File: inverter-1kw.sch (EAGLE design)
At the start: 190 parts, among them IC1 LMV358MMX, IC2 LMV358MMX, Q4 1200980569**TRANS SMD NPN MMB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, Q6 1200980569**TRANS SMD NPN MMB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, U1 ACS712, U4 ACS712, U5 SI8230, U6 SI8230, U7 ACS712, X2 https://ozdisan.com/connector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, X3 https://ozdisan.com/connector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, X7 https://ozdisan.com/connector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, X8 https://ozdisan.com/connector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

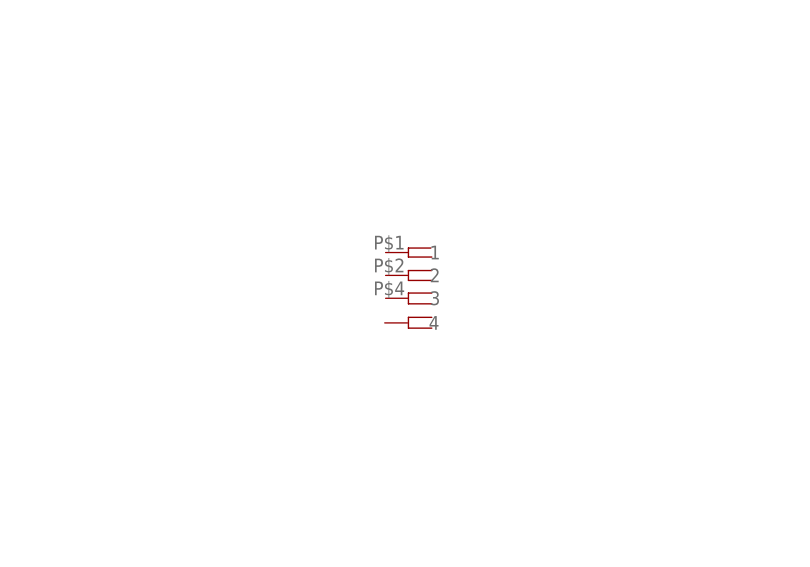
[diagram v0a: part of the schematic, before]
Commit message: Common Filter devresi düzenlendi
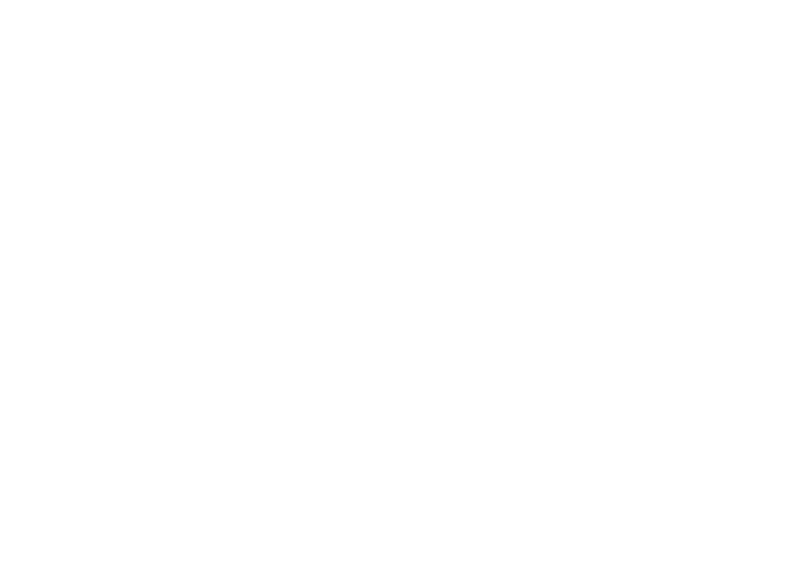
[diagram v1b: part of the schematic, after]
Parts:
- removed U$1: (no value), Andromeda:SCREWCONNECTORS(K93-01AH)
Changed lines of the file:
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@@
 <part name="C48" library="rcl" library_urn="urn:adsk.eagle:library:27228982" deviceset="C-EU" device="C1206" package3d_urn="urn:adsk.eagle:package:27228997/1"/>
 <part name="C49" library="rcl" library_urn="urn:adsk.eagle:library:27228982" deviceset="C-EU" device="C1206" package3d_urn="urn:adsk.eagle:package:27228997/1" value="22p"/>
-<part name="U$1" library="Andromeda" deviceset="SCREWCONNECTORS(K93-01AH)" device=""/>
 </parts>
 <sheets>
@@
 <attribute name="VALUE" x="494.284" y="88.011" size="1.778" layer="96"/>
 </instance>
-<instance part="U$1" gate="G$1" x="290.83" y="337.82" smashed="yes"/>
 </instances>
 <busses>

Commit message: Giris ve cikis guc terminalleri degistirildi.
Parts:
- removed X2, X3, X7, X8: https://ozdisan.com/connectors-and-interconnects/terminals/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, enko:RADE2
- added U$1, U$2, U$3, U$4: (no value), Andromeda:SCREWCONNECTORS(K93-01AH)
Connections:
- net AGND: now also U$2.1, U$2.2, U$2.3, U$2.4; no longer X8.1, X8.2
- net VA_OUT: now also U$4.1, U$4.2, U$4.3, U$4.4; no longer X3.1, X3.2
- net VB_OUT: now also U$3.1, U$3.2, U$3.3, U$3.4; no longer X2.1, X2.2
- net VSUPPLY+: now also U$1.1, U$1.2, U$1.3, U$1.4; no longer X7.1, X7.2

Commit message: Filtre devresi ve opamp devresi düzenlendi.
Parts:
- removed U$1, U$4: (no value), Andromeda:SCREWCONNECTORS(K93-01AH)
- added U$5, U$6: (no value), Andromeda:SCREWCONNECTORS(K93-01AH)
- renumbered U$3 to U$7
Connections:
- new net N$39: C32.-, C33.-, C35.-, C37.2, C40.-, C43.2, C47.2, C48.2, C49.2, C89.2, C90.2, GN4.S, LED5.C, R28.1, R67.1, R96.1, RGND1.2, U$5.1, U$5.2, U$5.3, U$5.4, U6.GNDB
- net AGND: no longer C32.-, C33.-, C35.-, C37.2, C40.-, C43.2, C47.2, C48.2, C49.2, C89.2, C90.2, GN4.S, LED5.C, R28.1, R67.1, R96.1, RGND1.2, U$2.1, U$2.2, U$2.3, U$2.4, U6.GNDB
- net VA_OUT: now also U$6.1, U$6.2, U$6.3, U$6.4; no longer U$4.1, U$4.2, U$4.3, U$4.4
- net VSUPPLY+: now also U$2.1, U$2.2, U$2.3, U$2.4; no longer U$1.1, U$1.2, U$1.3, U$1.4

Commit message: Soket baglantilari duzenlendi. B kol mosfetin AGND baglantisi duzeltildi.
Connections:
- removed net FAN: SV1.14
- removed net N$39: C32.-, C33.-, C35.-, C37.2, C40.-, C43.2, C47.2, C48.2, C49.2, C89.2, C90.2, GN4.S, LED5.C, R28.1, R67.1, R96.1, RGND1.2, U$5.1, U$5.2, U$5.3, U$5.4, U6.GNDB
- removed net N$83: R78.1, R79.2, U5.DISABLE
- removed net N$88: R84.1, R85.2, U6.DISABLE
- removed net NTC-HS1: SV1.16
- removed net NTC-HS2: SV1.18
- new net DRV1_EN: R78.1, R79.2, SV1.9, U5.DISABLE
- new net DRV2_EN: R84.1, R85.2, SV1.15, U6.DISABLE
- new net N$38: SV1.8
- net +3V3: now also SV1.17
- net +5V: now also SV1.19
- net AGND: now also C32.-, C33.-, C35.-, C37.2, C40.-, C43.2, C47.2, C48.2, C49.2, C89.2, C90.2, GN4.S, LED5.C, R28.1, R67.1, R96.1, RGND1.2, U$5.1, U$5.2, U$5.3, U$5.4, U6.GNDB
- net DGND: now also SV1.20
- net G11_PWM: now also SV1.5; no longer SV1.2
- net G12_PWM: now also SV1.7; no longer SV1.4
- net G13_PWM: now also SV1.11; no longer SV1.6
- net G14_PWM: now also SV1.13; no longer SV1.8
- net IA_SENS: now also SV1.14; no longer SV1.9
- net IB_SENS: now also SV1.18; no longer SV1.11
- net IIN_SENS: now also SV1.3; no longer SV1.5
- net RELAY1: now also SV1.2; no longer SV1.10
- net RELAY2: now also SV1.4; no longer SV1.12
- net VA_SENS: now also SV1.12; no longer SV1.13
- net VB_SENS: now also SV1.16; no longer SV1.15
- net VIN_SENS: now also SV1.1; no longer SV1.7
- net VIN_SENS_DIFF: now also SV1.10; no longer SV1.3
- net VOUT_SENS_DIFF: now also SV1.6; no longer SV1.1
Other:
- note added: "220AC"
- note removed: "Maks - 100V"

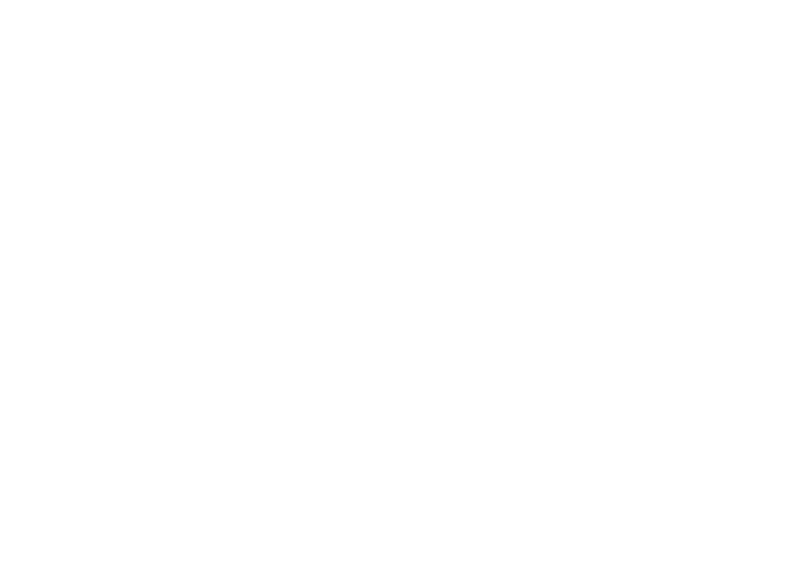
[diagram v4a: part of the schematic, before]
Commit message: ölçüm devresi düzenlendi
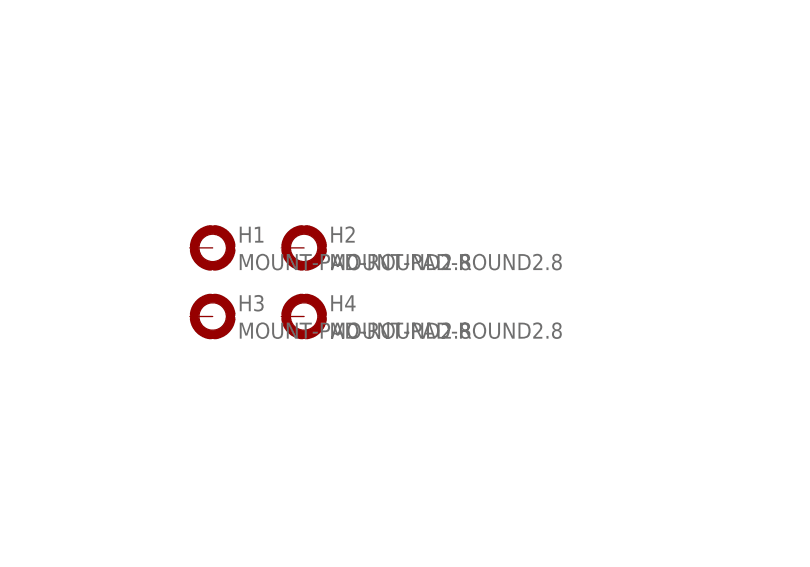
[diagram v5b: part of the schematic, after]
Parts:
- added H1, H2, H3, H4: MOUNT-PAD-ROUND2.8, holes:MOUNT-PAD-ROUND2.8
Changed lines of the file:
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@@
 <part name="U$6" library="Andromeda" library_urn="urn:adsk.eagle:library:27258842" deviceset="SCREWCONNECTORS(K93-01AH)" device="" package3d_urn="urn:adsk.eagle:package:27281814/2"/>
 <part name="U$7" library="Andromeda" library_urn="urn:adsk.eagle:library:27258842" deviceset="SCREWCONNECTORS(K93-01AH)" device="" package3d_urn="urn:adsk.eagle:package:27281814/2"/>
+<part name="H1" library="holes" library_urn="urn:adsk.eagle:library:237" deviceset="MOUNT-PAD-ROUND" device="2.8" package3d_urn="urn:adsk.eagle:package:14281/1"/>
+<part name="H2" library="holes" library_urn="urn:adsk.eagle:library:237" deviceset="MOUNT-PAD-ROUND" device="2.8" package3d_urn="urn:adsk.eagle:package:14281/1"/>
+<part name="H3" library="holes" library_urn="urn:adsk.eagle:library:237" deviceset="MOUNT-PAD-ROUND" device="2.8" package3d_urn="urn:adsk.eagle:package:14281/1"/>
+<part name="H4" library="holes" library_urn="urn:adsk.eagle:library:237" deviceset="MOUNT-PAD-ROUND" device="2.8" package3d_urn="urn:adsk.eagle:package:14281/1"/>
 </parts>
 <sheets>
@@
 <instance part="U$6" gate="G$1" x="816.61" y="226.06" smashed="yes"/>
 <instance part="U$7" gate="G$1" x="817.88" y="116.84" smashed="yes"/>
+<instance part="H1" gate="G$1" x="417.83" y="-13.97" smashed="yes">
+<attribute name="NAME" x="420.624" y="-13.3858" size="1.778" layer="95"/>
+<attribute name="VALUE" x="420.624" y="-16.4338" size="1.778" layer="96"/>
+</instance>
+<instance part="H2" gate="G$1" x="427.99" y="-13.97" smashed="yes">
+<attribute name="NAME" x="430.784" y="-13.3858" size="1.778" layer="95"/>
+<attribute name="VALUE" x="430.784" y="-16.4338" size="1.778" layer="96"/>
+</instance>
+<instance part="H3" gate="G$1" x="417.83" y="-21.59" smashed="yes">
+<attribute name="NAME" x="420.624" y="-21.0058" size="1.778" layer="95"/>
+<attribute name="VALUE" x="420.624" y="-24.0538" size="1.778" layer="96"/>
+</instance>
+<instance part="H4" gate="G$1" x="427.99" y="-21.59" smashed="yes">
+<attribute name="NAME" x="430.784" y="-21.0058" size="1.778" layer="95"/>
+<attribute name="VALUE" x="430.784" y="-24.0538" size="1.778" layer="96"/>
+</instance>
 </instances>
 <busses>

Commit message: Giris ve giris terminalleri soket yapildi. Ganlarin dibindeki capler sadelestirildi.
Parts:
- removed C43: (no value), rcl:C-EUC2220K
- removed D1, D2: (no value), diode:DIODE-SOD123
- removed Q4, Q6: 1200980569**TRANS SMD NPN MMBTA06 SOT-23 80V 500mA, transistor-npn:BC846ALT1SMD
- removed R32, R37, R42, R43: (no value), rcl:R-EU_0411/12
- removed R36, R41: (no value), rcl:R-EU_R0603
- removed RL1, RL2: 0417, Erelay:0417
- removed U$2, U$5, U$6, U$7: (no value), Andromeda:SCREWCONNECTORS(K93-01AH)
- added X1: GMSTBV3, con-phoenix-762:GMSTBV3
- added X2: MSTBV2, con-phoenix-508:MSTBV2
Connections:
- removed net N$14: C42.2, C43.1
- removed net N$22: C28.1, C30.2
- removed net N$32: C29.1, C36.2
- removed net N$33: C37.1, C41.2
- removed net N$44: D1.A, Q4.C, RL1G$1.2
- removed net N$45: Q4.B, R36.1
- removed net N$51: D2.A, Q6.C, RL2G$1.2
- removed net N$52: Q6.B, R41.1
- removed net N$55: R32.1, R37.1, R42.1, R43.1, RL1G$2.S
- removed net V_IN: C32.+, C33.+, C35.+, C40.+, R102.2, R28.2, R32.2, R37.2, R42.2, R43.2, R93.2, RL2G$2.S, U4.IP1+, U4.IP2+
- new net PE: H1.MOUNT, H2.MOUNT, H3.MOUNT, H4.MOUNT, X1-1.1
- net AGND: now also C30.2, C36.2, C41.2, C42.2, X1-3.1; no longer C43.2, U$5.1, U$5.2, U$5.3, U$5.4
- net DGND: no longer Q4.E, Q6.E
- net RELAY1: no longer R36.2
- net RELAY2: no longer R41.2
- net VA_OUT: now also X2-1.1; no longer U$6.1, U$6.2, U$6.3, U$6.4
- net VB_OUT: now also X2-2.1; no longer U$7.1, U$7.2, U$7.3, U$7.4
- net VDD: no longer D1.C, D2.C, RL1G$1.1, RL2G$1.1
- net VIN: now also C37.1; no longer C36.1, C41.1, C42.1
- net VSUPPLY+: now also C28.1, C29.1, C32.+, C33.+, C35.+, C36.1, C40.+, C41.1, C42.1, R102.2, R28.2, R93.2, U4.IP1+, U4.IP2+, X1-2.1; no longer RL1G$2.P, RL2G$2.P, U$2.1, U$2.2, U$2.3, U$2.4
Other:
- moved on the sheet: C28, C29, C30, C32, C33, C35, C36, C37, C40, C41, C42, H1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

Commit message: Negatif gerilim ihtiyacindan dolayi her bir ganfet icin izole DC-DC eklendi.
DC-DC gate-driver besleme gerilimleri VDD'ye baglandi.

Filtre bobinleri icin KS130 toroid nuvesi eklendi.
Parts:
- removed C136: 10u, rcl:C-USC1206
- removed C143, C144, C145: 0.1uF, rcl:C-USC0603
- removed C146: 10uF, rcl:C-USC0805
- removed C147: 22uF, rcl:C-USC1206
- removed C75, C76, C87, C88, C89, C90: 100n, rcl:C-USC0603
- removed D6: (no value), diode:DIODE-DO214AC
- removed L7: ARYA_COMMON_FILTER, enko:ARYA_COMMON_FILTER
- removed R70, R86: 10, rcl:R-US_R1206
- removed RGND, RGND1: 0, rcl:R-US_R0603
- added C43, C50, C54, C55, C60, C61, C67, C68: 1200920567**CAP 0603 CER 1uF 25V %10X7R, rcl:C-EUC0603K
- added C51, C56, C57, C62, C63, C64: 0.1uF, rcl:C-USC0603
- added C52, C58, C65: 10uF, rcl:C-USC0805
- added C53, C59, C66: 22uF, rcl:C-USC1206
- added C69, C70, C71, C74: 100n, rcl:C-EUC0603K
- added D1, D2, D3: (no value), diode:ZENER-DIODESOD80C
- added DC4, DC7: RI-0512S/P_DC_DC_5V_12V, my_parts1:RI-0512S/P_DC_DC_5V_12V
- added L3, L4, L5: ARYA_COMMON_FILTER, enko:ARYA_COMMON_FILTER
- added R32, R34, R35, R36: 10k, rcl:R-US_R0603
- added R37, R38, R39, R40: 2k2, rcl:R-US_R0603
- C25, C26: value 100n -> 0.1uF
- C27: value 10u -> 0.1uF; device rcl:C-USC1206 -> rcl:C-USC0603
- D5: device diode:DIODE-DO214AC -> diode:ZENER-DIODESOD80C
- L1, L2: value SFT1240 -> KS130-2PIN; device inductors:SFT1240 -> Andromeda:KS130-2PIN
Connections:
- removed net GND_DRV1: C140.2, C141.2, C27.2, L6.3, RGND.1
- removed net GND_DRV2: C136.2, C145.2, C146.2, L7.3, RGND1.1
- removed net N$131: C144.2, DC2.3.VOUT-, L7.2
- removed net N$132: C144.1, DC2.4.VOUT+, L7.1
- removed net N$77: D6.A, R86.1
- removed net VCC_1: C140.1, C141.1, C27.1, C75.1, C76.1, L6.4, R70.2, U5.VDDB
- removed net VCC_2: C136.1, C145.1, C146.1, C89.1, C90.1, L7.4, R86.2, U6.VDDB
- removed net VDDA: C25.1, C26.1, C87.1, C88.1, D5.C, D6.C, U5.VDDA, U6.VDDA
- new net N$14: C26.2, DC4.3.VOUT-, L3.2
- new net N$22: C56.1, DC2.4.VOUT+, L4.1
- new net N$32: C56.2, DC2.3.VOUT-, L4.2
- new net N$33: C63.1, DC7.4.VOUT+, L5.1
- new net N$39: C63.2, DC7.3.VOUT-, L5.2
- new net VG1_M: C140.2, C141.2, C50.2, C69.2, L6.3, R32.1, R40.1, U5.GNDA
- new net VG1_P: C140.1, C141.1, C43.1, C69.1, D5.C, L6.4, R40.2, U5.VDDA
- new net VG2_M: C51.2, C52.2, C55.2, C70.2, L3.3, R35.1, R39.1, U5.GNDB
- new net VG2_P: C51.1, C52.1, C54.1, C70.1, D1.C, L3.4, R39.2, U5.VDDB
- new net VG3_M: C57.2, C58.2, C61.2, C71.2, L4.3, R34.1, R38.1, U6.GNDA
- new net VG3_P: C57.1, C58.1, C60.1, C71.1, D2.C, L4.4, R38.2, U6.VDDA
- new net VG4_M: C64.2, C65.2, C68.2, C74.2, L5.3, R36.1, R37.1, U6.GNDB
- new net VG4_P: C64.1, C65.1, C67.1, C74.1, D3.C, L5.4, R37.2, U6.VDDB
- net +5V: no longer C138.1, C142.1, C143.1, C147.1, DC1.2.VIN+, DC2.2.VIN+
- net AGND: now also C54.2, C55.1, C67.2, C68.1, D1.A, D3.A, R35.2, R36.2; no longer C75.2, C76.2, C89.2, C90.2, RGND.2, RGND1.2, U5.GNDB, U6.GNDB
- net DGND: now also C25.2, C27.2, C53.2, C59.2, C62.2, C66.2, DC4.1.VIN-, DC7.1.VIN-; no longer C143.2, C147.2
- net N$3: now also C26.1, DC4.4.VOUT+, L3.1; no longer D5.A, R70.1
- net SW_LEG_A: now also C43.2, C50.1, D5.A, R32.2; no longer C25.2, C26.2, U5.GNDA
- net SW_LEG_B: now also C60.2, C61.1, D2.A, R34.2; no longer C87.2, C88.2, U6.GNDA
- net VDD: now also C138.1, C142.1, C25.1, C27.1, C53.1, C59.1, C62.1, C66.1, DC1.2.VIN+, DC2.2.VIN+, DC4.2.VIN+, DC7.2.VIN+
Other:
- note added: "Driver'a yakin olmali"
- moved on the sheet: C10, C11, C114, C12, C13, C138, C139, C14, C140, C141, C142, C15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
